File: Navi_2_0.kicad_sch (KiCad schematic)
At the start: 102 parts, among them J1 USB_B_Micro, J10 BAT-, J2 Conn_01x24_Male, J27 Micro_SD_Card_Det, J9 BAT+, Q1 DMG2301L-7, Q2 TF2310, Q3 DMG2301L-7, Q4 Q_NPN_BEC, Q5 Q_NPN_BEC, Q6 DMG2301L-7, Q7 DMG2301L-7, SW1 SW_Push, SW2 SW_Push, U1 MT3420C, U2 MT3420C, U3 ESP32-WROOM-32, U4 CH340K, U5 L96-M33, U6 LSM303AH, U7 TCN75-3.3

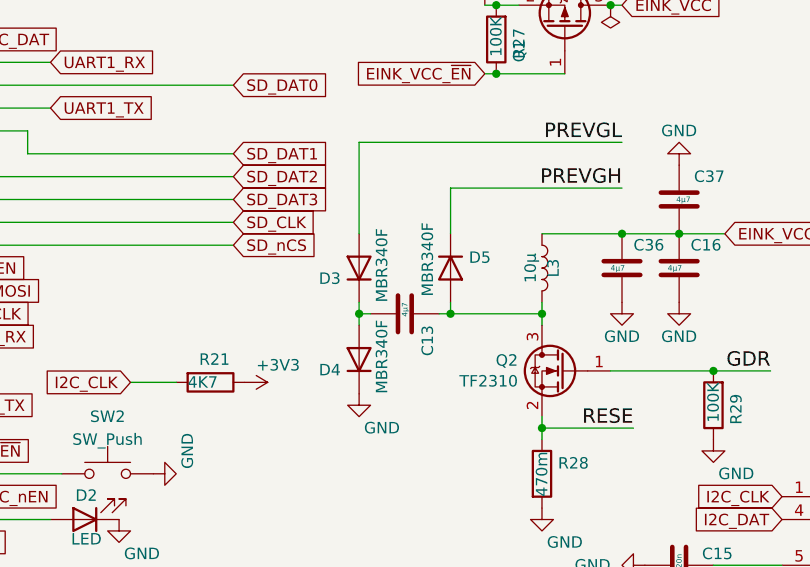
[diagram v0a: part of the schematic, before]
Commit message: Update BOM LCSC
Generated actual LCSC_BOM.csv to order parts on www.LCSC.com
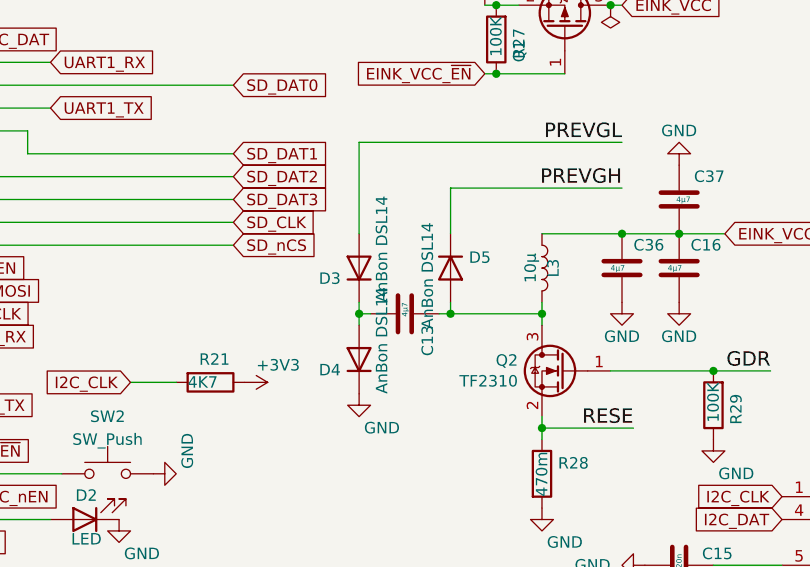
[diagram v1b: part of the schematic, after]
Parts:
- C1, C10, C11, C14, C16, C19, C2, C3, C31, C32, C33, C36, C37, C7: LCSC C307468 -> C415373
- C13, C24, C25: LCSC C513768 -> C77096
- D1: LCSC (none) -> C2827672
- D3, D4, D5: value MBR340F -> AnBon DSL14; LCSC C475721 -> C397616
- J2: LCSC (none) -> C283126
- J27: LCSC (none) -> ??
- Q4: LCSC (none) -> C181167
- R10: LCSC (none) -> C23208
- R12: LCSC (none) -> C170597
- R2, R3: LCSC (none) -> C105428
- R28: LCSC C270918 -> C25040
- SW1, SW2, U5, U6, U7: LCSC (none) -> !!
- U1, U2: LCSC (none) -> C181741
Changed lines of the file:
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@@
+      (effects (font (size 1.27 1.27)) hide)
+    )
+    (property "LCSC" "C105428" (id 4) (at 27.94 152.4 0)
       (effects (font (size 1.27 1.27)) hide)
     )
@@
       (effects (font (size 1.27 1.27)) hide)
     )
+    (property "LCSC" "C105428" (id 4) (at 27.94 176.53 0)
+      (effects (font (size 1.27 1.27)) hide)
+    )
     (pin "1")
     (pin "2")
@@
       (effects (font (size 1.27 1.27)) hide)
     )
+    (property "LCSC" "C23208" (id 4) (at 71.12 151.13 0)
+      (effects (font (size 1.27 1.27)) hide)
+    )
     (pin "1")
     (pin "2")
@@
       (effects (font (size 1.27 1.27)) hide)
     )
+    (property "LCSC" "C170597" (id 4) (at 71.12 175.26 0)
+      (effects (font (size 1.27 1.27)) hide)
+    )
     (pin "1")
     (pin "2")
@@
       (effects (font (size 1.27 1.27)) hide)
     )
-    (property "LCSC" "C270918" (id 4) (at 154.94 71.12 0)
+    (property "LCSC" "C25040" (id 4) (at 154.94 71.12 0)
       (effects (font (size 1.27 1.27)) hide)
     )
@@
       (effects (font (size 1.27 1.27)) (justify left))
     )
-    (property "Value" "MBR340F" (id 1) (at 137.16 52.07 0)
+    (property "Value" "AnBon DSL14" (id 1) (at 137.16 52.07 0)
       (effects (font (size 1.27 1.27)) (justify left))
     )
@@
       (effects (font (size 1.27 1.27)) hide)
     )
-    (property "LCSC" "C475721" (id 4) (at 134.62 48.26 90)
+    (property "LCSC" " 	C397616" (id 4) (at 134.62 48.26 90)
       (effects (font (size 1.27 1.27)) hide)
     )
@@
       (effects (font (size 1.27 1.27)) (justify left))
     )
-    (property "Value" "MBR340F" (id 1) (at 137.16 62.23 0)
+    (property "Value" "AnBon DSL14" (id 1) (at 137.16 62.23 0)
       (effects (font (size 1.27 1.27)) (justify left))
     )
@@
       (effects (font (size 1.27 1.27)) hide)
     )
-    (property "LCSC" "C475721" (id 4) (at 134.62 58.42 90)
+    (property "LCSC" " 	C397616" (id 4) (at 134.62 58.42 90)
       (effects (font (size 1.27 1.27)) hide)
     )
@@
       (effects (font (size 1.27 1.27)) (justify left))
     )
-    (property "Value" "MBR340F" (id 1) (at 142.24 43.18 0)
+    (property "Value" "AnBon DSL14" (id 1) (at 142.24 43.18 0)
       (effects (font (size 1.27 1.27)) (justify left))
     )
@@
       (effects (font (size 1.27 1.27)) hide)
     )
-    (property "LCSC" "C475721" (id 4) (at 144.78 48.26 90)
+    (property "LCSC" " 	C397616" (id 4) (at 144.78 48.26 90)
       (effects (font (size 1.27 1.27)) hide)
     )
@@
       (effects (font (size 1.27 1.27)) hide)
     )
-    (property "LCSC" "C307468" (id 4) (at 17.78 151.13 0)
+    (property "LCSC" "C415373" (id 4) (at 17.78 151.13 0)
       (effects (font (size 1.27 1.27)) hide)
     )
@@
       (effects (font (size 1.27 1.27)) hide)
     )
-    (property "LCSC" "C307468" (id 4) (at 17.78 175.26 0)
+    (property "LCSC" "C415373" (id 4) (at 17.78 175.26 0)
       (effects (font (size 1.27 1.27)) hide)
     )
@@
       (effects (font (size 1.27 1.27)) hide)
     )
-    (property "LCSC" "C307468" (id 4) (at 39.37 43.18 0)
+    (property "LCSC" "C415373" (id 4) (at 39.37 43.18 0)
       (effects (font (size 1.27 1.27)) hide)
     )
@@
       (effects (font (size 1.27 1.27)) hide)
     )
-    (property "LCSC" "C307468" (id 4) (at 41.91 86.36 0)
+    (property "LCSC" "C415373" (id 4) (at 41.91 86.36 0)
       (effects (font (size 1.27 1.27)) hide)
     )
@@
       (effects (font (size 1.27 1.27)) hide)
     )
-    (property "LCSC" "C307468" (id 4) (at 77.47 151.13 0)
+    (property "LCSC" "C415373" (id 4) (at 77.47 151.13 0)
       (effects (font (size 1.27 1.27)) hide)
     )
@@
       (effects (font (size 1.27 1.27)) hide)
     )
-    (property "LCSC" "C307468" (id 4) (at 77.47 175.26 0)
+    (property "LCSC" "C415373" (id 4) (at 77.47 175.26 0)
       (effects (font (size 1.27 1.27)) hide)
     )
@@
       (effects (font (size 1.27 1.27)) hide)
     )
-    (property "LCSC" "C513768" (id 4) (at 139.7 53.34 0)
+    (property "LCSC" "C77096" (id 4) (at 139.7 53.34 0)
       (effects (font (size 1.27 1.27)) hide)
     )
@@
       (effects (font (size 1.27 1.27)) hide)
     )
-    (property "LCSC" "C307468" (id 4) (at 163.83 48.26 0)
+    (property "LCSC" "C415373" (id 4) (at 163.83 48.26 0)
       (effects (font (size 1.27 1.27)) hide)
     )
@@
       (effects (font (size 1.27 1.27)) hide)
     )
-    (property "LCSC" "C307468" (id 4) (at 166.37 156.21 0)
+    (property "LCSC" "C415373" (id 4) (at 166.37 156.21 0)
       (effects (font (size 1.27 1.27)) hide)
     )
@@
       (effects (font (size 1.27 1.27)) hide)
     )
-    (property "LCSC" "C307468" (id 4) (at 170.18 40.64 0)
+    (property "LCSC" "C415373" (id 4) (at 170.18 40.64 0)
       (effects (font (size 1.27 1.27)) hide)
     )
@@
       (effects (font (size 1.27 1.27)) hide)
     )
-    (property "LCSC" "C307468" (id 4) (at 170.18 48.26 0)
+    (property "LCSC" "C415373" (id 4) (at 170.18 48.26 0)
       (effects (font (size 1.27 1.27)) hide)
     )
@@
       (effects (font (size 1.27 1.27)) hide)
     )
-    (property "LCSC" "C307468" (id 4) (at 170.18 146.05 0)
+    (property "LCSC" "C415373" (id 4) (at 170.18 146.05 0)
       (effects (font (size 1.27 1.27)) hide)
     )
@@
       (effects (font (size 1.27 1.27)) hide)
     )
-    (property "LCSC" "C307468" (id 4) (at 175.26 146.05 0)
+    (property "LCSC" "C415373" (id 4) (at 175.26 146.05 0)
       (effects (font (size 1.27 1.27)) hide)
     )
@@
       (effects (font (size 1.27 1.27)) hide)
     )
-    (property "LCSC" "C307468" (id 4) (at 199.39 130.81 0)
+    (property "LCSC" "C415373" (id 4) (at 199.39 130.81 0)
       (effects (font (size 1.27 1.27)) hide)
     )
@@
       (effects (font (size 1.27 1.27)) hide)
     )
-    (property "LCSC" "C307468" (id 4) (at 219.71 90.17 0)
+    (property "LCSC" "C415373" (id 4) (at 219.71 90.17 0)
       (effects (font (size 1.27 1.27)) hide)
     )
@@
       (effects (font (size 1.27 1.27)) hide)
     )
-    (property "LCSC" "C513768" (id 4) (at 242.57 22.86 0)
+    (property "LCSC" "C77096" (id 4) (at 242.57 22.86 0)
       (effects (font (size 1.27 1.27)) hide)
     )
@@
       (effects (font (size 1.27 1.27)) hide)
     )
-    (property "LCSC" "C513768" (id 4) (at 242.57 27.94 0)
+    (property "LCSC" "C77096" (id 4) (at 242.57 27.94 0)
       (effects (font (size 1.27 1.27)) hide)
     )
@@
     )
     (property "Datasheet" "C412365" (id 3) (at 22.86 27.94 0)
+      (effects (font (size 1.27 1.27)) hide)
+    )
+    (property "LCSC" "!!" (id 4) (at 27.94 27.94 0)
       (effects (font (size 1.27 1.27)) hide)
     )
@@
       (effects (font (size 1.27 1.27)) hide)
     )
+    (property "LCSC" "!!" (id 4) (at 106.68 71.12 0)
+      (effects (font (size 1.27 1.27)) hide)
+    )
     (pin "1")
     (pin "2")
@@
     )
     (property "Datasheet" "~" (id 3) (at 121.92 110.49 0)
+      (effects (font (size 1.27 1.27)) hide)
+    )
+    (property "LCSC" "C181167" (id 4) (at 121.92 110.49 0)
       (effects (font (size 1.27 1.27)) hide)
     )
@@
     )
     (property "Datasheet" "www.st.com/resource/en/datasheet/esda6v1-5sc6.pdf" (id 3) (at 36.83 110.49 90)
+      (effects (font (size 1.27 1.27)) hide)
+    )
+    (property "LCSC" "C2827672" (id 4) (at 36.83 110.49 0)
       (effects (font (size 1.27 1.27)) hide)
     )
@@
       (effects (font (size 1.27 1.27)) hide)
     )
+    (property "LCSC" "C181741" (id 4) (at 41.91 149.86 0)
+      (effects (font (size 1.27 1.27)) hide)
+    )
     (pin "1")
     (pin "2")
@@
       (effects (font (size 1.27 1.27)) hide)
     )
+    (property "LCSC" "C181741" (id 4) (at 41.91 173.99 0)
+      (effects (font (size 1.27 1.27)) hide)
+    )
     (pin "1")
     (pin "2")
@@
     )
     (property "Datasheet" "~" (id 3) (at 270.51 48.26 0)
+      (effects (font (size 1.27 1.27)) hide)
+    )
+    (property "LCSC" "C283126" (id 4) (at 270.51 48.26 0)
       (effects (font (size 1.27 1.27)) hide)
     )
@@
       (effects (font (size 1.27 1.27)) hide)
     )
+    (property "LCSC" "!!" (id 4) (at 213.36 52.07 0)
+      (effects (font (size 1.27 1.27)) hide)
+    )
     (pin "1")
     (pin "2")
@@
     )
     (property "Datasheet" "https://www.st.com/en/mems-and-sensors/lsm303ah.html" (id 3) (at 199.39 97.79 0)
+      (effects (font (size 1.27 1.27)) hide)
+    )
+    (property "LCSC" "!!" (id 4) (at 196.85 81.28 0)
       (effects (font (size 1.27 1.27)) hide)
     )
@@
       (effects (font (size 1.27 1.27)) hide)
     )
+    (property "LCSC" "??" (id 4) (at 255.27 129.54 0)
+      (effects (font (size 1.27 1.27)) hide)
+    )
     (pin "1")
     (pin "10")
@@
     (property "DESCRIPTION" "L96 is a concurrent multi-GNSS receiver module with embedded chip antenna. With 33 tracking channels, 99 acquisition channels and 210 PRN channels, L96 supports concurrent reception of up to three GNSS systems _GPS+GLONASS+Galileo_" (id 9) (at 139.7 170.18 0)
       (effects (font (size 1.27 1.27)) (justify left bottom) hide)
+    )
+    (property "LCSC" "!!" (id 10) (at 139.7 170.18 0)
+      (effects (font (size 1.27 1.27)) hide)
     )
     (pin "10")
@@
     )
     (path "/00000000-0000-0000-0000-000060b22b10"
-      (reference "D3") (unit 1) (value "MBR340F") (footprint "Diode_SMD:D_SOD-123F")
+      (reference "D3") (unit 1) (value "AnBon DSL14") (footprint "Diode_SMD:D_SOD-123F")
     )
     (path "/00000000-0000-0000-0000-000060b218c5"
-      (reference "D4") (unit 1) (value "MBR340F") (footprint "Diode_SMD:D_SOD-123F")
+      (reference "D4") (unit 1) (value "AnBon DSL14") (footprint "Diode_SMD:D_SOD-123F")
     )
     (path "/00000000-0000-0000-0000-0000602ea629"
-      (reference "D5") (unit 1) (value "MBR340F") (footprint "Diode_SMD:D_SOD-123F")
+      (reference "D5") (unit 1) (value "AnBon DSL14") (footprint "Diode_SMD:D_SOD-123F")
     )
     (path "/00000000-0000-0000-0000-000060e05b1b"
